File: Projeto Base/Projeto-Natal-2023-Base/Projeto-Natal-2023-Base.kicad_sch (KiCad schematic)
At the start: 39 parts, among them J1 Conn_01x03_Pin, U1 CH32V003F4P6

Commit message: Draft 1
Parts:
- removed D1, D13, D5, D9: LED R, LED_THT:LED_D5.0mm, symbol Device:LED
- removed D10, D14, D2, D6: LED G, LED_THT:LED_D5.0mm, symbol Device:LED
- removed D11, D15, D3, D7: LED B, LED_THT:LED_D5.0mm, symbol Device:LED
- removed D12, D16, D4, D8: LED Y, LED_THT:LED_D5.0mm, symbol Device:LED

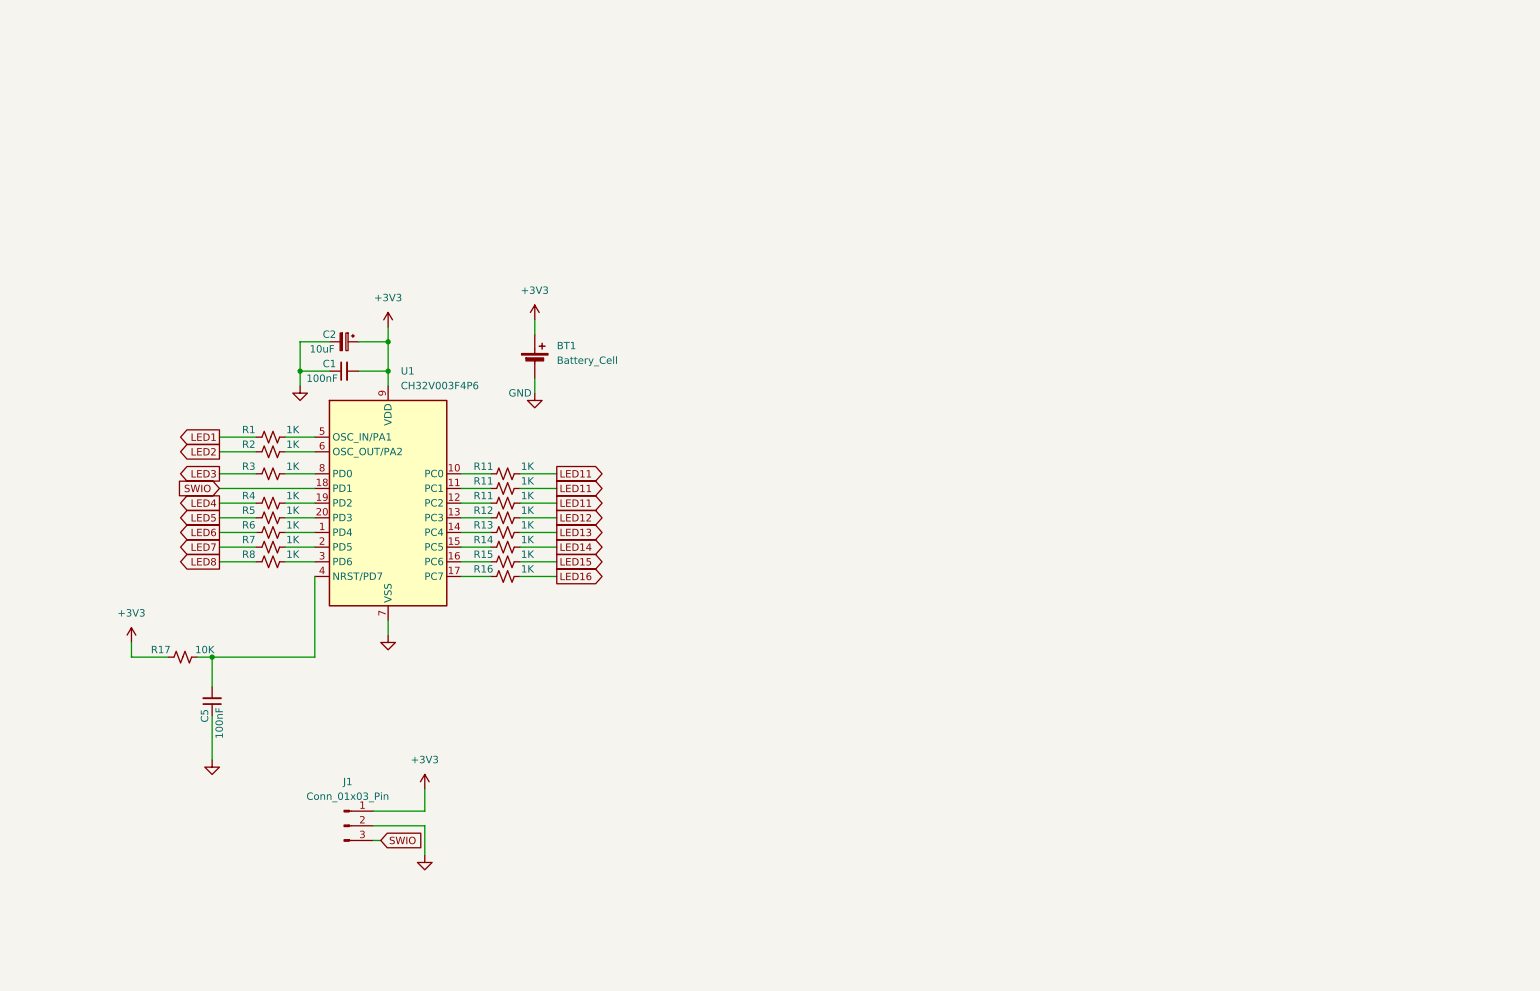
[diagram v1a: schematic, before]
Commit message: posicionando os componentes
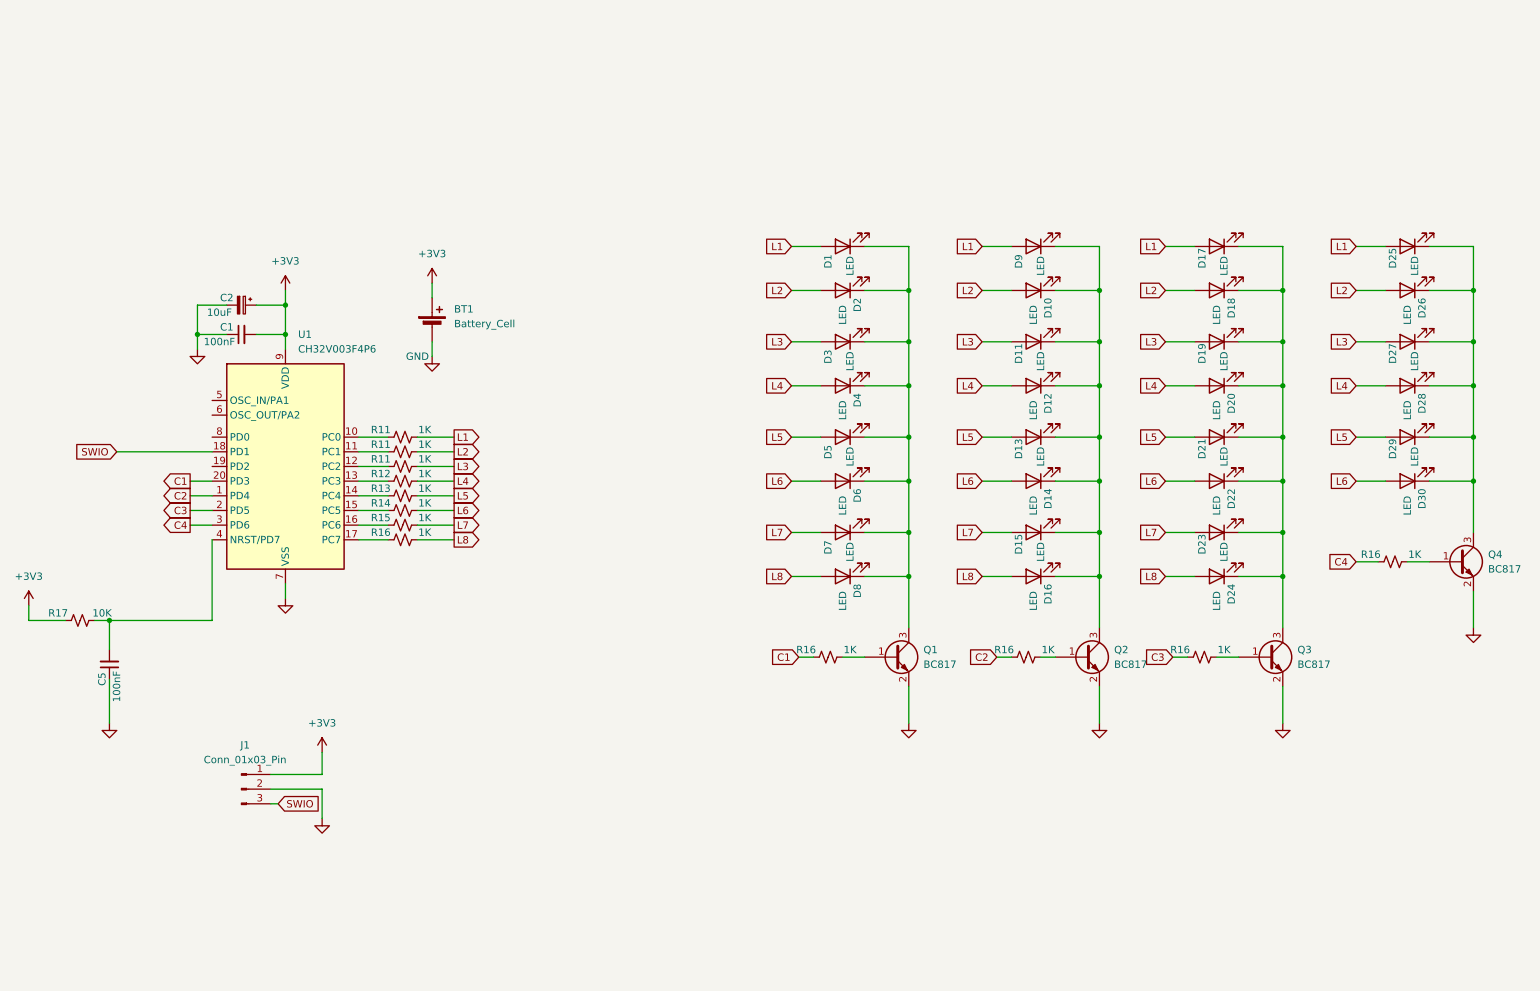
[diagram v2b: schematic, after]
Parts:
- removed R1, R2, R3, R4, R5, R6, R7, R8: 1K, Resistor_SMD:R_0603_1608Metric_Pad0.98x0.95mm_HandSolder, symbol Device:R_Small_US
- added D1, D10, D11, D12, D13, D14, D15, D16, D17, D18, D19, D2, D20, D21, D22, D23, D24, D25, D26, D27, D28, D29, D3, D30, D4, D5, D6, D7, D8, D9: LED, LED_SMD:LED_0805_2012Metric, symbol Device:LED
- added Q1, Q2, Q3, Q4: BC817, Package_TO_SOT_SMD:SOT-23, symbol Transistor_BJT:BC817
- added R16 (x4): 1K, Resistor_SMD:R_0603_1608Metric_Pad0.98x0.95mm_HandSolder, symbol Device:R_Small_US
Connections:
- net GND: now also Q1.2 (E), Q2.2 (E), Q3.2 (E), Q4.2 (E)
- net C3: now reaches U1.2 (PD5)
- net C3: now also R16.1
- net C1: now reaches U1.20 (PD3)
- net C1: now also R16.1
- net C2: now reaches U1.1 (PD4)
- net C2: now also R16.1
- net C4: now reaches U1.3 (PD6)
- net C4: now also R16.1
- removed net LED11: R11.2, R11.2, R11.2
- net LED12 renamed L4
- net L4: now also D12.2 (A), D20.2 (A), D28.2 (A), D4.2 (A)
- net LED13 renamed L5
- net L5: now also D13.2 (A), D21.2 (A), D29.2 (A), D5.2 (A)
- net LED14 renamed L6
- net L6: now also D14.2 (A), D22.2 (A), D30.2 (A), D6.2 (A)
- net LED15 renamed L7
- net L7: now also D15.2 (A), D23.2 (A), D7.2 (A)
- net LED16 renamed L8
- net L8: now also D16.2 (A), D24.2 (A), D8.2 (A)
- new net: D1.1 (K), D2.1 (K), D3.1 (K), D4.1 (K), D5.1 (K), D6.1 (K), D7.1 (K), D8.1 (K), Q1.3 (C)
- new net: D17.1 (K), D18.1 (K), D19.1 (K), D20.1 (K), D21.1 (K), D22.1 (K), D23.1 (K), D24.1 (K), Q3.3 (C)
- new net: D25.1 (K), D26.1 (K), D27.1 (K), D28.1 (K), D29.1 (K), D30.1 (K), Q4.3 (C)
- new net: D10.1 (K), D11.1 (K), D12.1 (K), D13.1 (K), D14.1 (K), D15.1 (K), D16.1 (K), D9.1 (K), Q2.3 (C)
- new net: Q3.1 (B), R16.2
- new net: Q1.1 (B), R16.2
- new net: Q4.1 (B), R16.2
- new net: Q2.1 (B), R16.2
- new net L1: D1.2 (A), D17.2 (A), D25.2 (A), D9.2 (A), R11.2
- new net L2: D10.2 (A), D18.2 (A), D2.2 (A), D26.2 (A), R11.2
- new net L3: D11.2 (A), D19.2 (A), D27.2 (A), D3.2 (A), R11.2
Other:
- moved on the sheet: BT1, C1, C2, C5, J1, R11, R12, R13, R14, R15, R16, R17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

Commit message: routing...
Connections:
- net L1: now also D22.2 (A), D30.2 (A); no longer D17.2 (A), D25.2 (A)
- net L2: now also D21.2 (A), D29.2 (A); no longer D18.2 (A), D26.2 (A)
- net L3: now also D20.2 (A), D28.2 (A); no longer D19.2 (A), D27.2 (A)
- net L4: now also D19.2 (A), D27.2 (A); no longer D20.2 (A), D28.2 (A)
- net L5: now also D18.2 (A), D26.2 (A); no longer D21.2 (A), D29.2 (A)
- net L6: now also D17.2 (A), D25.2 (A); no longer D22.2 (A), D30.2 (A)
- net L7: now also D16.2 (A), D24.2 (A); no longer D23.2 (A)
- net L8: now also D23.2 (A); no longer D16.2 (A), D24.2 (A)
- net at D17.1 (K), D18.1 (K), D19.1 (K)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: now also D16.1 (K); no longer D23.1 (K), D24.1 (K)
- net at D25.1 (K), D26.1 (K), D27.1 (K)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: now also D23.1 (K), D24.1 (K)
- net at D10.1 (K), D11.1 (K), D12.1 (K)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: no longer D16.1 (K)
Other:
- moved on the sheet: D16, D17, D18, D19, D20, D21, D22, D25, D26, D27, D28, D29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

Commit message: v1.0.0
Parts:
- removed J1: Conn_01x03_Pin, Connector_PinHeader_2.54mm:PinHeader_1x03_P2.54mm_Vertical, symbol Connector:Conn_01x03_Pin
- added BZ1: Buzzer, Library:PassiveBuzzerSMD_JiangsuHuaneng_MLT-5030, symbol Device:Buzzer
- added J1, J2, J3, J4: Conn_01x01_Pin, TestPoint:TestPoint_Pad_D2.0mm, symbol Connector:Conn_01x01_Pin
- added Q5: MMBT3906, Package_TO_SOT_SMD:SOT-23, symbol Transistor_BJT:MMBT3906
- added R16: 1K, Resistor_SMD:R_0603_1608Metric_Pad0.98x0.95mm_HandSolder, symbol Device:R_Small_US
- added SW1: SW_Push, Button_Switch_SMD:SW_Push_1P1T_NO_6x6mm_H9.5mm, symbol Switch:SW_Push
- BT1: footprint Battery:BatteryHolder_Keystone_3002_1x2032 -> Battery:BatteryHolder_Multicomp_BC-2001_1x2032
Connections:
- net +3V3: now also J2.1 (Pin_1), Q5.2 (E)
- net GND: now also BZ1.1 (-), J3.1 (Pin_1), SW1.2
- net SWIO: now also J4.1 (Pin_1)
- net BZR: now reaches U1.19 (PD2)
- net BZR: now also R16.2
- net BT: now reaches U1.8 (PD0)
- net BT: now also SW1.1
- new net: Q5.1 (B), R16.1
- new net: BZ1.2 (+), Q5.3 (C)
- no-connect marks 0 -> 3

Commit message: Versão para revisão
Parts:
- BT1: value Battery_Cell -> BC-2001
- BZ1: value Buzzer -> MLT-5030
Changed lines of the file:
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@@
       (effects (font (size 1.27 1.27)) (justify left))
     )
-    (property "Value" "Battery_Cell" (at 91.44 76.8985 0)
+    (property "Value" "BC-2001" (at 91.44 76.8985 0)
       (effects (font (size 1.27 1.27)) (justify left))
     )
@@
       (effects (font (size 1.27 1.27)) hide)
     )
-    (property "Datasheet" "~" (at 87.63 75.946 90)
+    (property "Datasheet" "https://octopart.com/bc-2001-multicomp-21274013" (at 87.63 75.946 90)
       (effects (font (size 1.27 1.27)) hide)
     )
@@
       (effects (font (size 1.27 1.27)) hide)
     )
-    (property "Datasheet" "~" (at 115.57 149.86 0)
+    (property "Datasheet" "https://www.lcsc.com/product-detail/Tactile-Switches_Made-in-China-C23873_C23873.html" (at 115.57 149.86 0)
       (effects (font (size 1.27 1.27)) hide)
     )
@@
       (effects (font (size 1.27 1.27)))
     )
-    (property "Value" "Buzzer" (at 34.8049 46.99 0)
+    (property "Value" "MLT-5030" (at 34.8049 46.99 0)
       (effects (font (size 1.27 1.27)))
     )
@@
       (effects (font (size 1.27 1.27)) hide)
     )
-    (property "Datasheet" "~" (at 36.195 54.61 90)
-      (effects (font (size 1.27 1.27)) hide)
-    )
+    (property "Datasheet" "https://jlcpcb.com/partdetail/Jiangsu_HuanengElec-MLT5030/C95297" (at 36.195 54.61 90)
+      (effects (font (size 1.27 1.27)) hide)
+    )

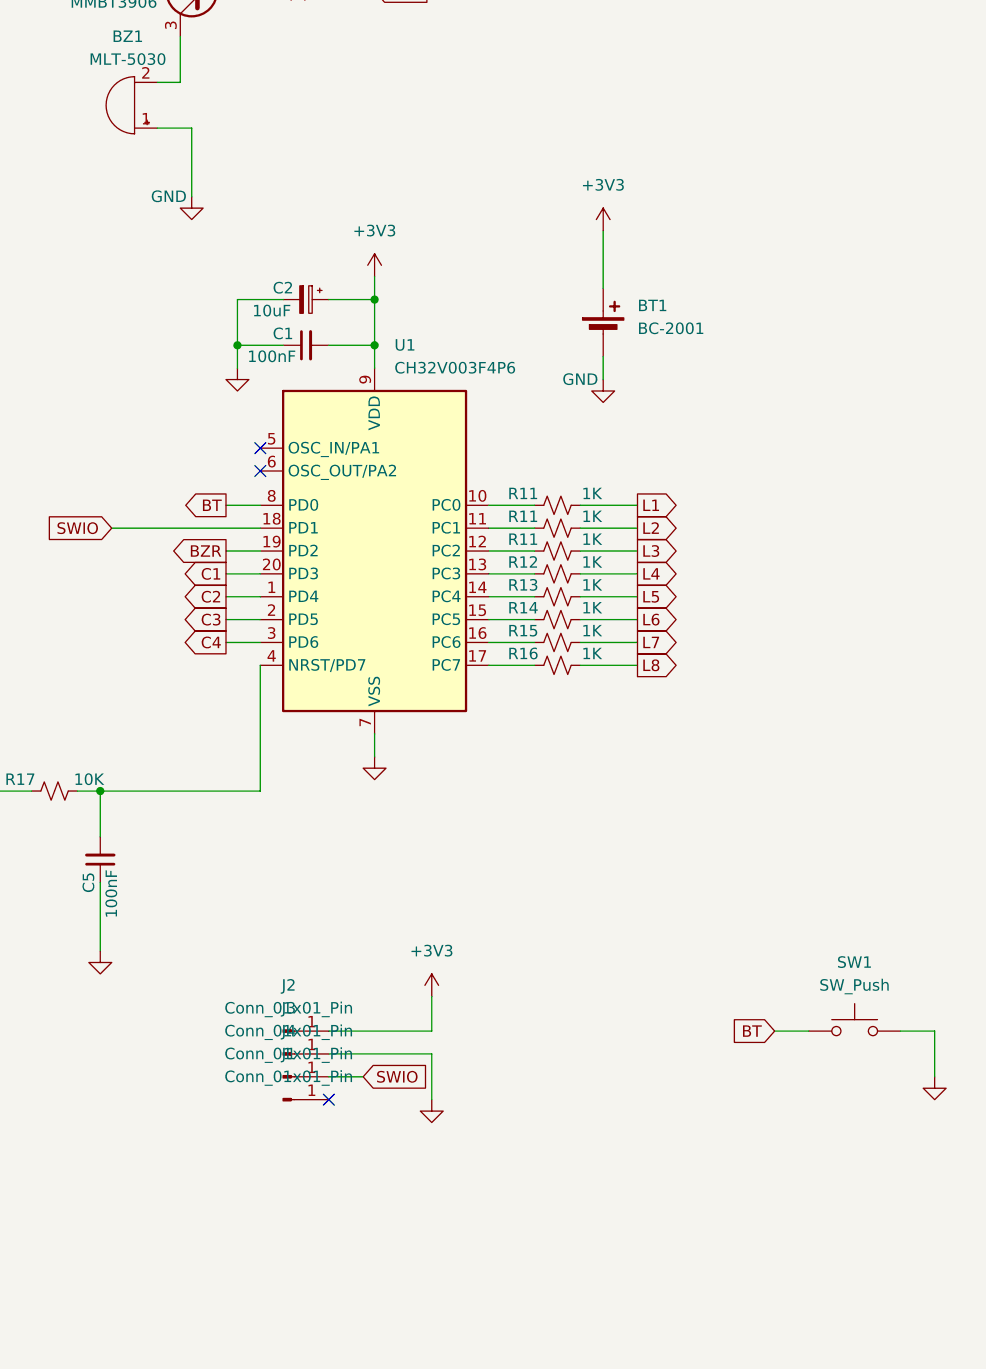
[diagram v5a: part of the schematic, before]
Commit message: Adicionando pinos extras e resistor de pullup para o BT
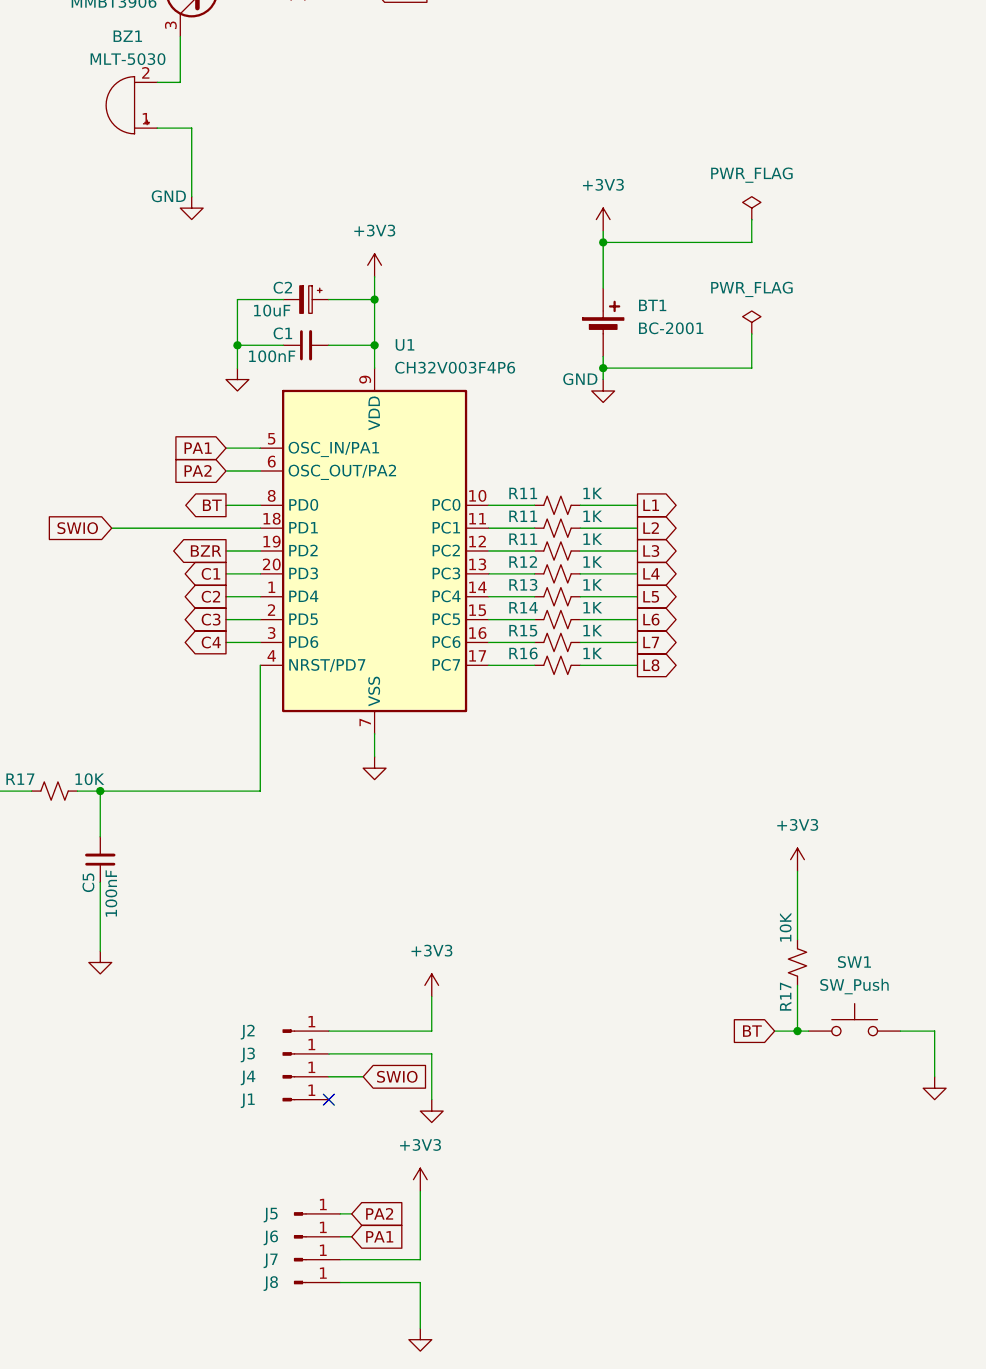
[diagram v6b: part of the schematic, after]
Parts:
- added J5, J6, J7, J8: Conn_01x01_Pin, TestPoint:TestPoint_Pad_D1.0mm, symbol Connector:Conn_01x01_Pin
- added R17: 10K, Resistor_SMD:R_0603_1608Metric_Pad0.98x0.95mm_HandSolder, symbol Device:R_Small_US
- J1, J2, J3, J4: footprint TestPoint:TestPoint_Pad_D2.0mm -> TestPoint:TestPoint_Pad_D1.5mm
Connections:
- net +3V3: now also J7.1 (Pin_1), R17.2
- net BT: now also R17.1
- net GND: now also J8.1 (Pin_1)
- net PA1: now reaches U1.5 (OSC_IN/PA1)
- net PA1: now also J6.1 (Pin_1)
- net PA2: now reaches U1.6 (OSC_OUT/PA2)
- net PA2: now also J5.1 (Pin_1)
- no-connect marks 3 -> 1
